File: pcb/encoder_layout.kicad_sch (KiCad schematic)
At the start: 11 parts, among them Q8 AO3400A

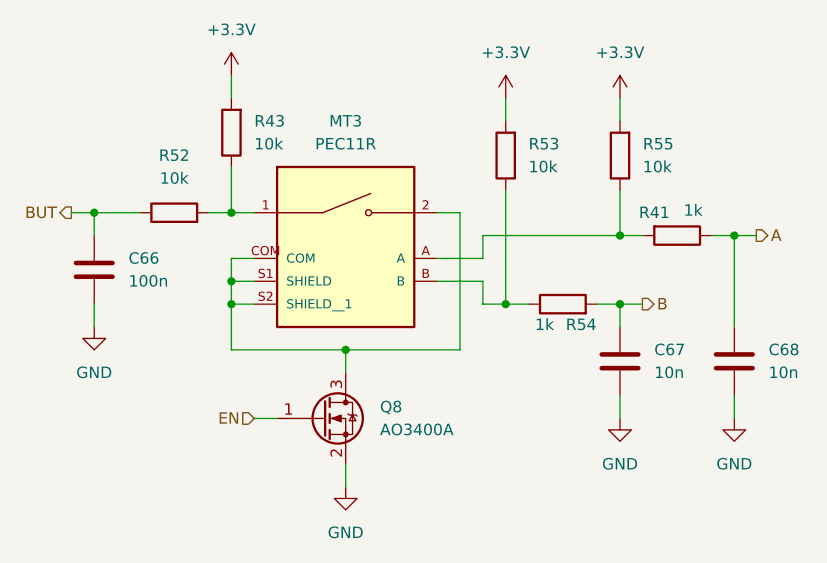
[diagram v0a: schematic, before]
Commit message: refactor: removed the laser component of the project
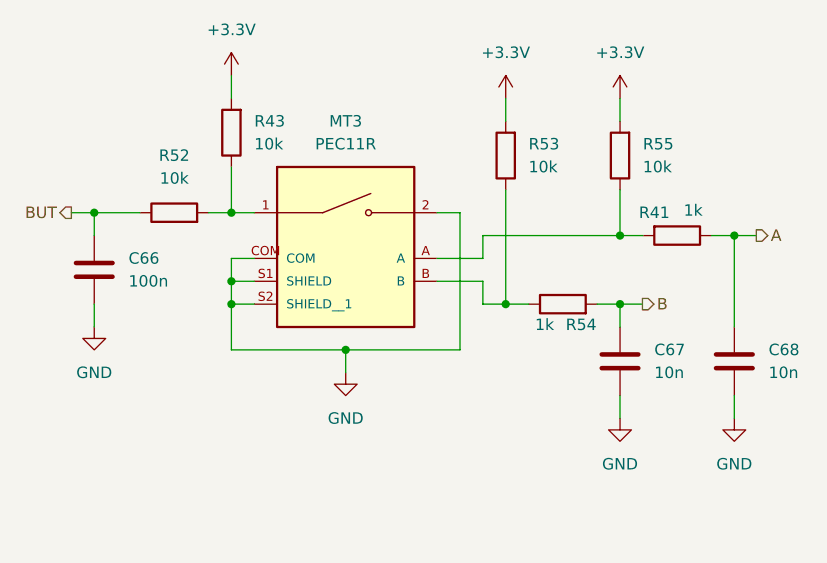
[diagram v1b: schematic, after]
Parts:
- removed Q8: AO3400A, Package_TO_SOT_SMD:SOT-23, symbol Transistor_FET:AO3400A
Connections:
- net GND: now also MT3.2, MT3.COM, MT3.S1 (SHIELD), MT3.S2 (SHIELD__1)
